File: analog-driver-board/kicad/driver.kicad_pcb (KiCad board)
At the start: 2 copper layers, 81.3 x 30.5 mm, 17 parts, among them J3 Barrel_Jack, J4 Barrel_Jack, J5 Conn_01x04, J7 Conn_01x02, U2 LDD-1500L

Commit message: remove wisconsin crest logo
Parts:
- removed G***: LOGO, footprints:logo

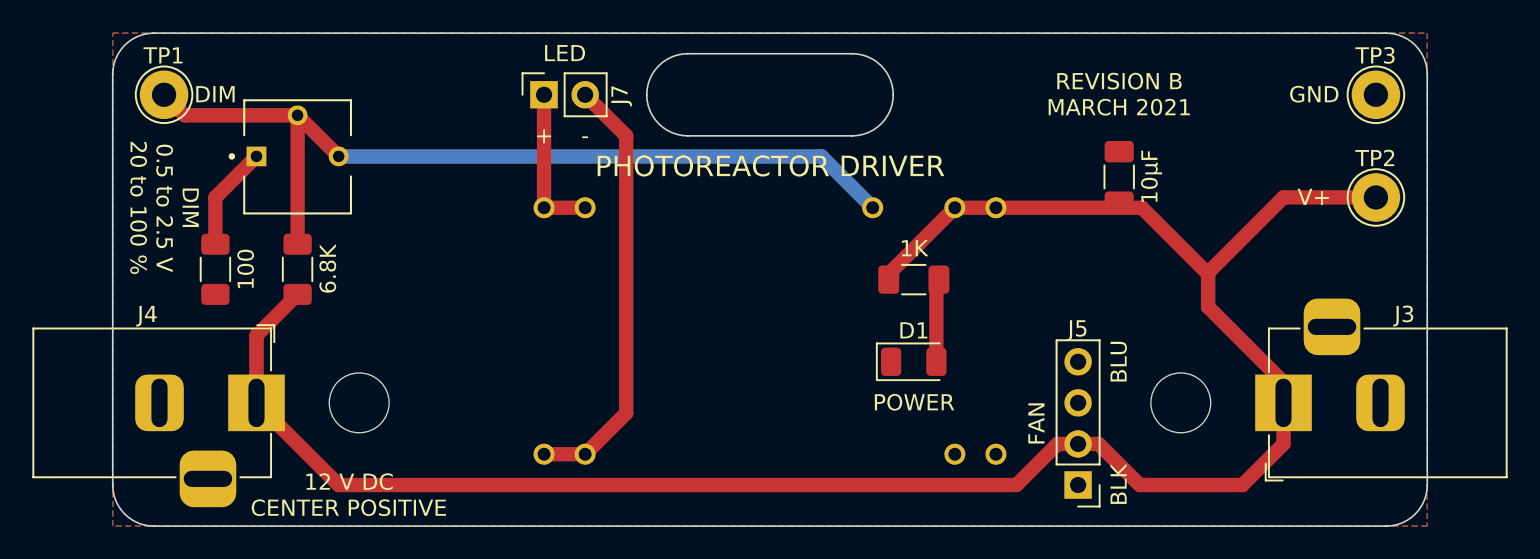
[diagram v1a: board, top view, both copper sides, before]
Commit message: add url to analog driver board
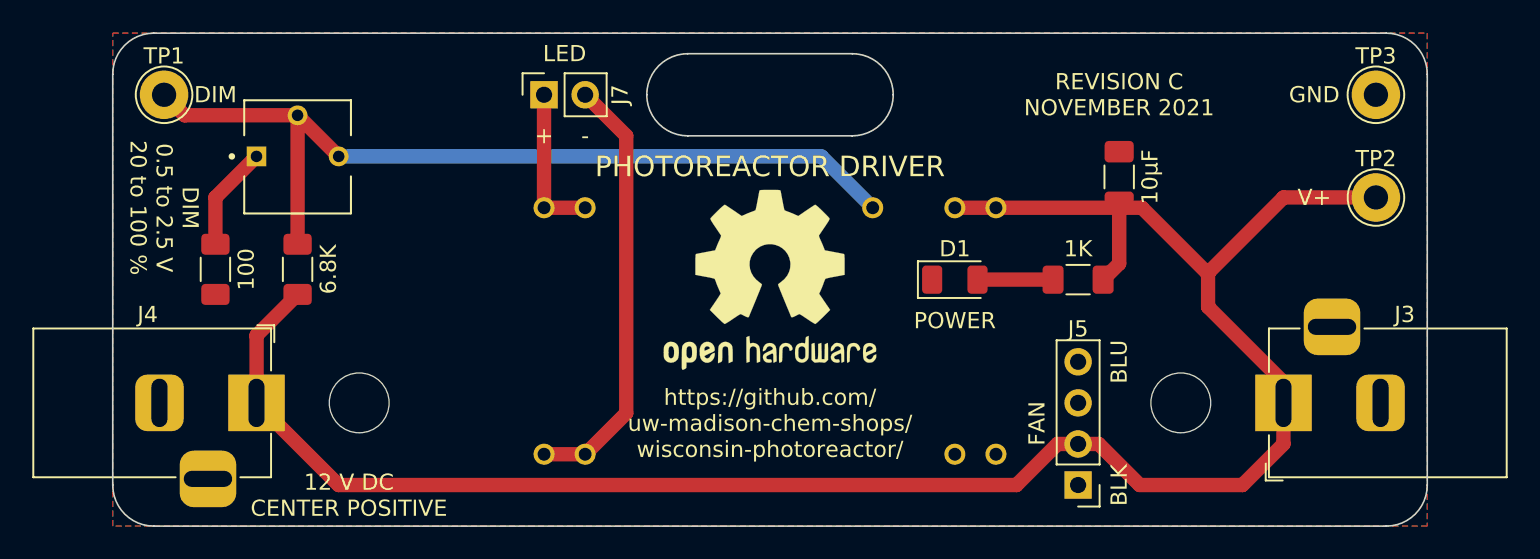
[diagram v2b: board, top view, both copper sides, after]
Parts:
- added REF**: OSHW-Logo2_14.6x12mm_SilkScreen, Symbol:OSHW-Logo2_14.6x12mm_SilkScreen, F.Cu at (127.0, 94.0)
- moved R5 10.2 mm to (146.1, 94.0), turned to 180 degrees
- moved D1 5.68 mm to (138.4, 94.0)
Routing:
- net +12V: track 126.1 -> 125.2 mm
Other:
- board text added: "REVISION C NOVEMBER 2021"
- board text added: "https://github.com/ uw-madison-chem-shops/ wisconsin-photoreactor/"
- board text removed: "REVISION B MARCH 2021"
